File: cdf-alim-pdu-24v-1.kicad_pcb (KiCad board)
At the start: 2 copper layers, 80 x 60 mm, 130 parts, among them J1 Conn_01x02, J10 Conn_01x02, J11 Conn_01x02, J12 Conn_01x02, J13 Conn_01x02, J14 Conn_01x02, J15 Conn_01x02, J16 Conn_01x02, J17 Conn_01x02, J2 Conn_01x02, J3 Conn_01x02, J4 Conn_01x02, J5 Conn_01x02, J6 Conn_01x02, J7 Conn_01x02, J8 Conn_01x02, J9 Conn_01x02, Q1 BSC019N04LS, Q2 BSC019N04LS, Q3 BSC019N04LS, U1 TPS25983, U2 TPS25983, U3 TPS25983, U4 HT753-1, U5 MX25947, U6 MX25947, U7 MX25947

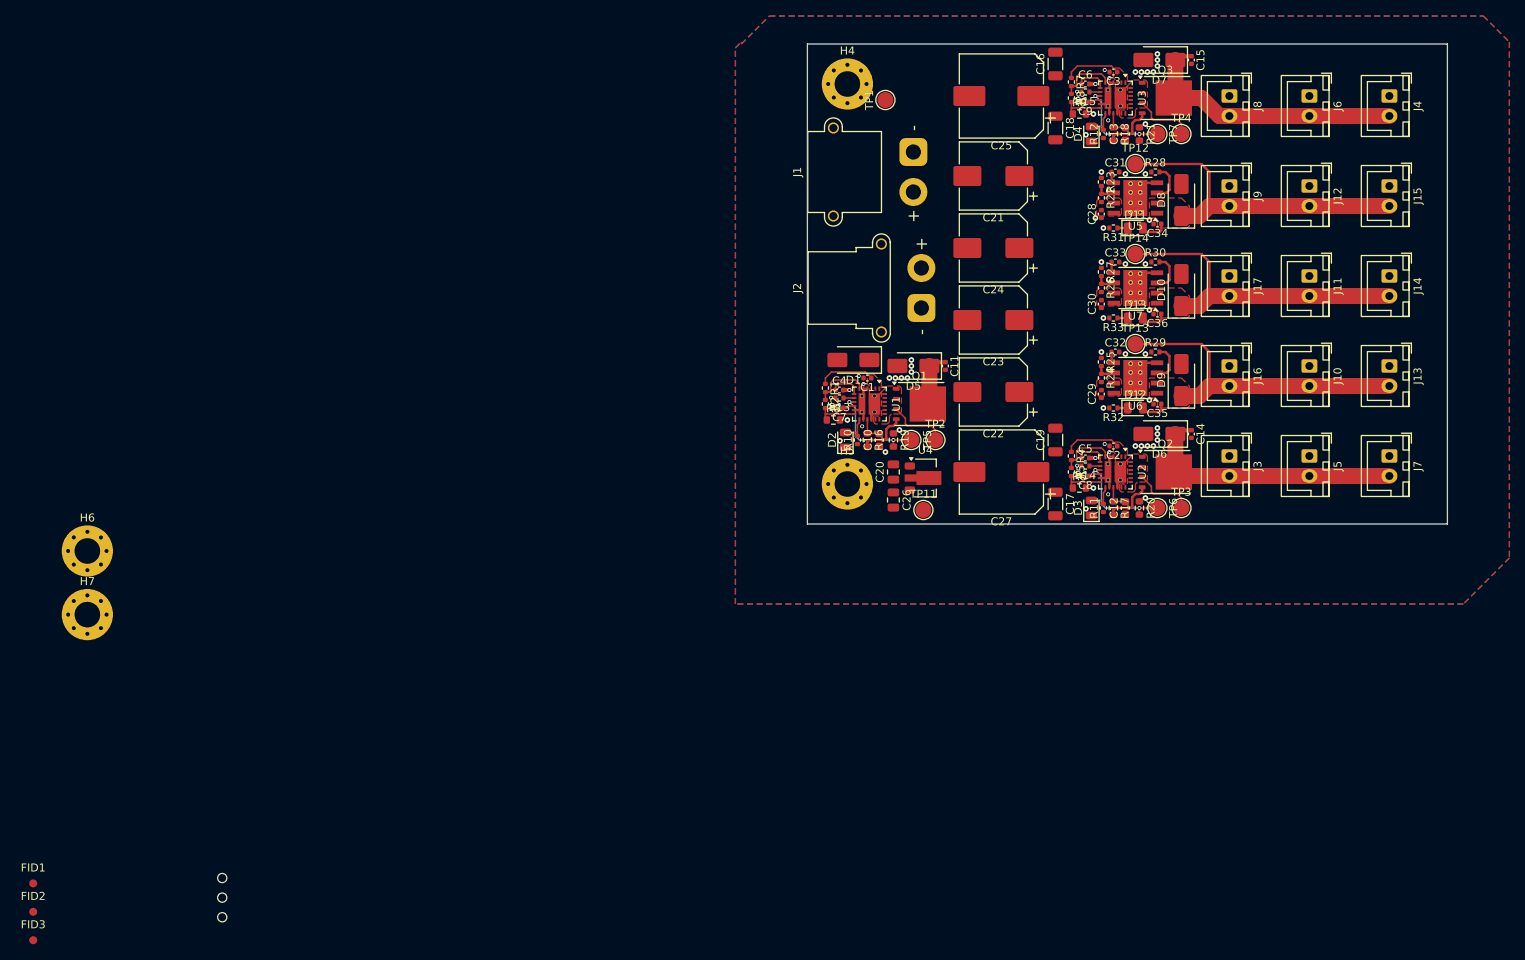
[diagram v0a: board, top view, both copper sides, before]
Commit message: pcb: add board outline
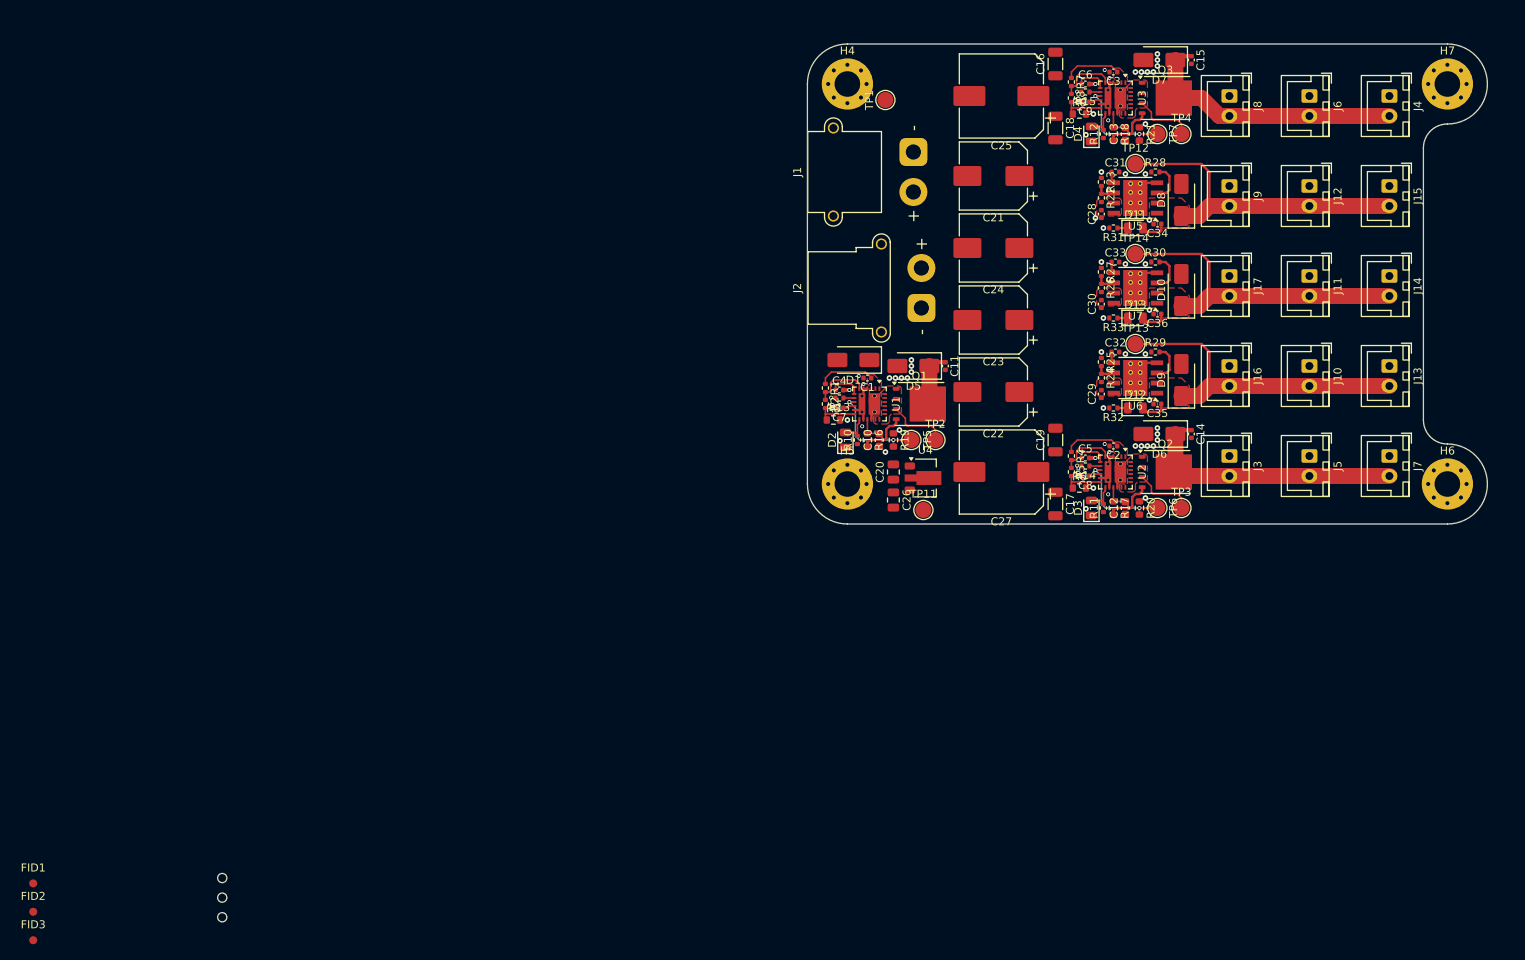
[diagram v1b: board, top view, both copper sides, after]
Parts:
- moved H7 182.5 mm to (240.0, 85.0)
- moved H6 170.2 mm to (240.0, 135.0)
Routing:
- removed copper zone on B.Cu, net GND
- removed copper zone on F.Cu, net GND
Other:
- board size 80 x 60 mm -> 85 x 60 mm
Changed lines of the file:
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@@
 	(footprint "MountingHole:MountingHole_3.2mm_M3_Pad_Via"
 		(layer "F.Cu")
-		(at 69.995 143.375)
+		(at 240 135)
 		(descr "Mounting Hole 3.2mm, M3, generated by kicad-footprint-generator mountinghole.py")
 		(tags "mountinghole M3")
@@
 	(footprint "MountingHole:MountingHole_3.2mm_M3_Pad_Via"
 		(layer "F.Cu")
-		(at 69.995 151.325)
+		(at 240 85)
 		(descr "Mounting Hole 3.2mm, M3, generated by kicad-footprint-generator mountinghole.py")
 		(tags "mountinghole M3")
@@
 		(embedded_fonts no)
 	)
-	(gr_rect
-		(start 160 80)
+	(gr_arc
+		(start 160 85)
+		(mid 161.464466 81.464466)
+		(end 165 80)
+		(stroke
+			(width 0.05)
+			(type default)
+		)
+		(layer "Edge.Cuts")
+	)
+	(gr_line
+		(start 160 135)
+		(end 160 85)
+		(stroke
+			(width 0.05)
+			(type default)
+		)
+		(layer "Edge.Cuts")
+	)
+	(gr_line
+		(start 165 80)
+		(end 240 80)
+		(stroke
+			(width 0.05)
+			(type default)
+		)
+		(layer "Edge.Cuts")
+	)
+	(gr_arc
+		(start 165 140)
+		(mid 161.464466 138.535534)
+		(end 160 135)
+		(stroke
+			(width 0.05)
+			(type default)
+		)
+		(layer "Edge.Cuts")
+	)
+	(gr_arc
+		(start 237 93)
+		(mid 237.87868 90.87868)
+		(end 240 90)
+		(stroke
+			(width 0.05)
+			(type default)
+		)
+		(layer "Edge.Cuts")
+	)
+	(gr_line
+		(start 237 127)
+		(end 237 93)
+		(stroke
+			(width 0.05)
+			(type default)
+		)
+		(layer "Edge.Cuts")
+	)
+	(gr_arc
+		(start 240 80)
+		(mid 243.535534 81.464466)
+		(end 245 85)
+		(stroke
+			(width 0.05)
+			(type default)
+		)
+		(layer "Edge.Cuts")
+	)
+	(gr_arc
+		(start 240 130)
+		(mid 237.87868 129.12132)
+		(end 237 127)
+		(stroke
+			(width 0.05)
+			(type default)
+		)
+		(layer "Edge.Cuts")
+	)
+	(gr_arc
+		(start 240 130)
+		(mid 243.535534 131.464466)
+		(end 245 135)
+		(stroke
+			(width 0.05)
+			(type default)
+		)
+		(layer "Edge.Cuts")
+	)
+	(gr_line
+		(start 240 140)
+		(end 165 140)
+		(stroke
+			(width 0.05)
+			(type default)
+		)
+		(layer "Edge.Cuts")
+	)
+	(gr_arc
+		(start 245 85)
+		(mid 243.535534 88.535534)
+		(end 240 90)
+		(stroke
+			(width 0.05)
+			(type default)
+		)
+		(layer "Edge.Cuts")
+	)
+	(gr_arc
+		(start 245 135)
+		(mid 243.535534 138.535534)
 		(end 240 140)
-		(radius 5)
 		(stroke
 			(width 0.05)
-			(type solid)
+			(type default)
 		)
-		(fill no)
 		(layer "Edge.Cuts")
 	)
@@
 			)
 		)
-	)
-	(zone
-		(net "GND")
-		(layers "F.Cu" "B.Cu")
-		(hatch edge 0.5)
-		(priority 2)
-		(connect_pads
-			(clearance 0.5)
-		)
-		(min_thickness 0.25)
-		(fill yes
-			(thermal_gap 0.5)
-			(thermal_bridge_width 0.5)
-			(island_removal_mode 0)
-		)
-		(polygon
-			(pts
-				(xy 244.5 76.5) (xy 247.75 79.75) (xy 247.75 144.25) (xy 242 150) (xy 151 150) (xy 151 80.5) (xy 151.75 79.75)
-				(xy 151.75 80) (xy 155.25 76.5)
-			)
-		)
